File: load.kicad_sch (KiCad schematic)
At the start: 0 parts

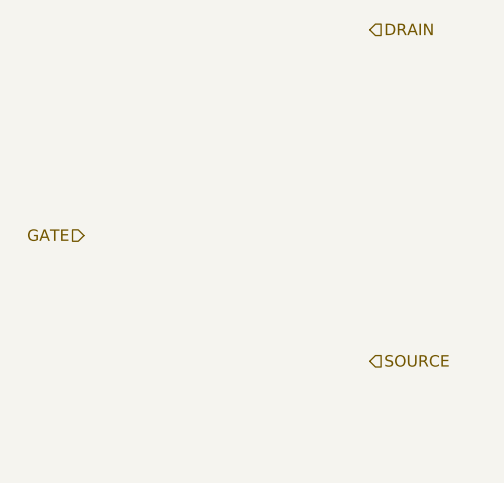
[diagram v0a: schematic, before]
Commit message: Added discharge Mosfet.
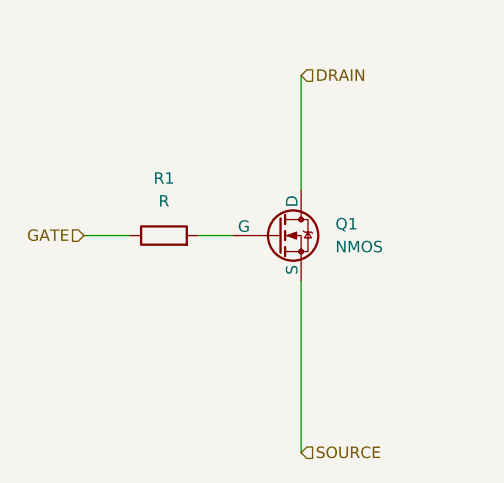
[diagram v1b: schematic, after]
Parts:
- added Q1: NMOS, symbol Simulation_SPICE:NMOS
- added R1: R, 100, symbol Device:R
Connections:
- net DRAIN: now also Q1.1 (D)
- net GATE: now also R1.1
- net SOURCE: now also Q1.3 (S)
- new net: Q1.2 (G), R1.2
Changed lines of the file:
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@@
 	(generator_version "8.0")
 	(paper "A4")
+	(wire
+		(pts
+			(xy 73.66 40.64) (xy 73.66 53.34)
+		)
+		(stroke
+			(width 0)
+			(type default)
+		)
+	)
+	(wire
+		(pts
+			(xy 73.66 63.5) (xy 73.66 82.55)
+		)
+		(stroke
+			(width 0)
+			(type default)
+		)
+	)
+	(wire
+		(pts
+			(xy 49.53 58.42) (xy 54.61 58.42)
+		)
+		(stroke
+			(width 0)
+			(type default)
+		)
+	)
+	(wire
+		(pts
+			(xy 62.23 58.42) (xy 66.04 58.42)
+		)
+		(stroke
+			(width 0)
+			(type default)
+		)
+	)
 	(hierarchical_label "SOURCE"
 		(shape input)
-		(at 81.28 72.39 0)
+		(at 73.66 82.55 0)
 		(fields_autoplaced yes)
 		(effects
@@
 	(hierarchical_label "DRAIN"
 		(shape input)
-		(at 81.28 35.56 0)
+		(at 73.66 40.64 0)
 		(fields_autoplaced yes)
 		(effects
@@
 		)
 	)
+	(symbol
+		(lib_id "Simulation_SPICE:NMOS")
+		(at 71.12 58.42 0)
+		(unit 1)
+		(exclude_from_sim no)
+		(in_bom yes)
+		(on_board yes)
+		(dnp no)
+		(fields_autoplaced yes)
+		(property "Reference" "Q1"
+			(at 77.47 57.1499 0)
+			(effects
+				(font
+					(size 1.27 1.27)
+				)
+				(justify left)
+			)
+		)
+		(property "Value" "NMOS"
+			(at 77.47 59.6899 0)
+			(effects
+				(font
+					(size 1.27 1.27)
+				)
+				(justify left)
+			)
+		)
+		(property "Footprint" ""
+			(at 76.2 55.88 0)
+			(effects
+				(font
+					(size 1.27 1.27)
+				)
+				(hide yes)
+			)
+		)
+		(property "Datasheet" "https://ngspice.sourceforge.io/docs/ngspice-html-manual/manual.xhtml#cha_MOSFETs"
+			(at 71.12 71.12 0)
+			(effects
+				(font
+					(size 1.27 1.27)
+				)
+				(hide yes)
+			)
+		)
+		(property "Description" "N-MOSFET transistor, drain/source/gate"
+			(at 71.12 58.42 0)
+			(effects
+				(font
+					(size 1.27 1.27)
+				)
+				(hide yes)
+			)
+		)
+		(property "Sim.Device" "NMOS"
+			(at 71.12 75.565 0)
+			(effects
+				(font
+					(size 1.27 1.27)
+				)
+				(hide yes)
+			)
+		)
+		(property "Sim.Type" "VDMOS"
+			(at 71.12 77.47 0)
+			(effects
+				(font
+					(size 1.27 1.27)
+				)
+				(hide yes)
+			)
+		)
+		(property "Sim.Pins" "1=D 2=G 3=S"
+			(at 71.12 73.66 0)
+			(effects
+				(font
+					(size 1.27 1.27)
+				)
+				(hide yes)
+			)
+		)
+		(pin "2"
+		)
+		(pin "3"
+		)
+		(pin "1"
+		)
+		(instances
+			(project ""
+				(path "/3a2a22aa-6e8a-41f2-9388-8b5b5cbcd4ba/d1647cf3-2c7f-4bb4-a193-2f331a3c09e1"
+					(reference "Q1")
+					(unit 1)
+				)
+			)
+		)
+	)
+	(symbol
+		(lib_id "Device:R")
+		(at 58.42 58.42 90)
+		(unit 1)
+		(exclude_from_sim no)
+		(in_bom yes)
+		(on_board yes)
+		(dnp no)
+		(fields_autoplaced yes)
+		(property "Reference" "R1"
+			(at 58.42 52.07 90)
+			(effects
+				(font
+					(size 1.27 1.27)
+				)
+			)
+		)
+		(property "Value" "R"
+			(at 58.42 54.61 90)
+			(effects
+				(font
+					(size 1.27 1.27)
+				)
+			)
+		)
+		(property "Footprint" "100"
+			(at 58.42 60.198 90)
+			(effects
+				(font
+					(size 1.27 1.27)
+				)
+				(hide yes)
+			)
+		)
+		(property "Datasheet" "~"
+			(at 58.42 58.42 0)
+			(effects
+				(font
+					(size 1.27 1.27)
+				)
+				(hide yes)
+			)
+		)
+		(property "Description" "Resistor"
+			(at 58.42 58.42 0)
+			(effects
+				(font
+					(size 1.27 1.27)
+				)
+				(hide yes)
+			)
+		)
+		(pin "1"
+		)
+		(pin "2"
+		)
+		(instances
+			(project ""
+				(path "/3a2a22aa-6e8a-41f2-9388-8b5b5cbcd4ba/d1647cf3-2c7f-4bb4-a193-2f331a3c09e1"
+					(reference "R1")
+					(unit 1)
+				)
+			)
+		)
+	)

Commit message: Prepared STS1_BATT_TEST.
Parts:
- Q1: value NMOS -> IPP050N03LF2S; footprint (none) -> Package_TO_SOT_THT:TO-220-3_Horizontal_TabUp
- R1: value R -> 100; footprint 100 -> Capacitor_SMD:C_0805_2012Metric_Pad1.18x1.45mm_HandSolder
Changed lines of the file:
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@@
 			)
 		)
-		(property "Value" "NMOS"
+		(property "Value" "IPP050N03LF2S"
 			(at 77.47 59.6899 0)
 			(effects
@@
 			)
 		)
-		(property "Footprint" ""
+		(property "Footprint" "Package_TO_SOT_THT:TO-220-3_Horizontal_TabUp"
 			(at 76.2 55.88 0)
 			(effects
@@
 			)
 		)
-		(property "Datasheet" "https://ngspice.sourceforge.io/docs/ngspice-html-manual/manual.xhtml#cha_MOSFETs"
+		(property "Datasheet" "https://www.mouser.at/datasheet/2/196/Infineon_IPP050N03LF2S_DataSheet_v02_00_EN-3476269.pdf"
 			(at 71.12 71.12 0)
 			(effects
@@
 			)
 		)
-		(property "Value" "R"
+		(property "Value" "100"
 			(at 58.42 54.61 90)
 			(effects
@@
 			)
 		)
-		(property "Footprint" "100"
+		(property "Footprint" "Capacitor_SMD:C_0805_2012Metric_Pad1.18x1.45mm_HandSolder"
 			(at 58.42 60.198 90)
 			(effects
